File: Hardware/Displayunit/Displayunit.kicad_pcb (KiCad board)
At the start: 4 copper layers, 155 x 64.8 mm, 137 parts, among them IC1 TSC2007, IC2 MX25LM51245GXDI00, IC3 IS66WVH8M8BLL-100B1LI_0, J1 615008138221, J2 615008138221, J3 54104-4031, J4 Conn_ARM_JTAG_SWD_20, J5 52271-0679, J6 Conn_02x06_Odd_Even, J7 WAGO_Klemmleiste_2-pol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

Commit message: PCB Prototypen Produktions Stand
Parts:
- removed C60, C61: 2u2, Capacitor_SMD:C_1210_3225Metric
- C62, C63: footprint Capacitor_SMD:C_1210_3225Metric -> Capacitor_SMD:C_0603_1608Metric
- U5: value TPS54160DGQR -> (none)
- moved R22 45.9 mm to (99.5, 87.3)
- moved C65 42.5 mm to (100.5, 84.8), turned to 270 degrees
- moved D7 37.8 mm to (96.1, 80.8), turned to 180 degrees
- moved C63 37.2 mm to (89.5, 80.5), turned to 90 degrees
- moved C62 35.9 mm to (89.4, 68.0), turned to 90 degrees
- moved R2 34.4 mm to (105.6, 74.3), turned to 270 degrees
- moved C64 32.3 mm to (100.4, 71.9), turned to 270 degrees
- moved D6 30.2 mm to (96.2, 67.6), turned to 180 degrees
- moved R21 30.1 mm to (99.4, 74.5)
- moved C37 7.92 mm to (97.0, 98.0), turned to 270 degrees
- moved R16 7.59 mm to (105.4, 86.2)
- moved C44 7.39 mm to (109.6, 87.0), turned to 0 degrees
- moved C58 6.36 mm to (98.7, 84.7), turned to 270 degrees
- moved C42 6.26 mm to (108.4, 74.8)
- moved C57 5.94 mm to (98.7, 71.9), turned to 270 degrees
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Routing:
- net GND: track 860.3 -> 895.1 mm, vias 99 -> 107
- net Net-(C40-Pad1): track 0.00 -> 17.7 mm, vias 0 -> 2
- net Net-(C41-Pad1): track 1.65 -> 16.5 mm, vias 0 -> 2
- net +3.3VA: track 154.3 -> 143.7 mm, vias 10 -> 11
- net PWR_Reset: track 0.00 -> 10.6 mm, vias 0 -> 2
- net Net-(R16-Pad2): track 1.91 -> 12.4 mm
- net +3V3: track 408.3 -> 400.6 mm, vias 36 -> 40
- net Net-(BT1-Pad1): track 41.3 -> 34.1 mm
- net +BATT: track 48.8 -> 55.3 mm
- net Net-(C27-Pad1): track 18.4 -> 24.3 mm
- net Net-(C38-Pad1): track 0.00 -> 5.72 mm
- net RESET: track 96.7 -> 101.5 mm, vias 5 -> 7
- net Net-(C57-Pad2): track 0.00 -> 4.58 mm
- net Net-(R14-Pad2): track 1.91 -> 6.46 mm
- net Net-(C58-Pad2): track 0.00 -> 4.35 mm
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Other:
- board text added: "(c) RFguy 03/2020"
- board text removed: "(c) RFguy 02/2020"

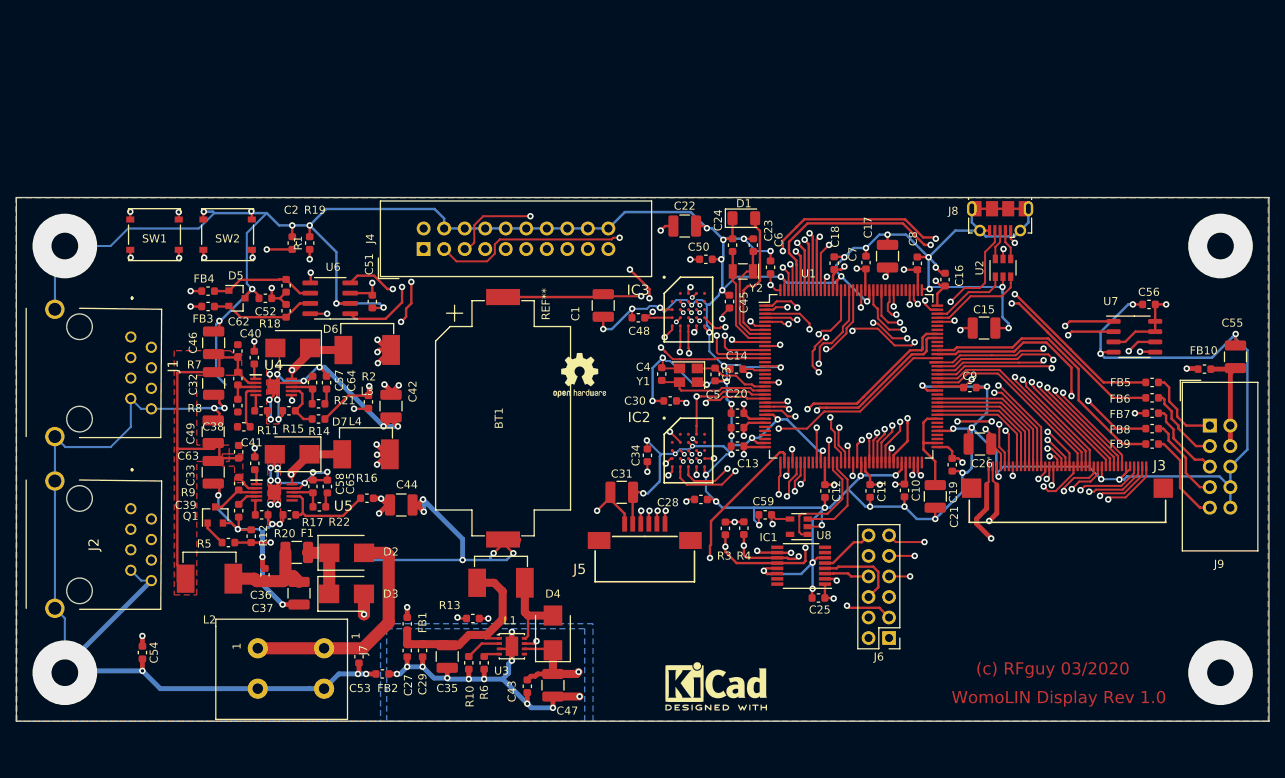
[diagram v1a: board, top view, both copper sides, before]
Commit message: Display Board: Fix JTAG REF, LED Treiber > TPS61165, Spulen zurück auf XAL4040 Footprint, Auf Version 2.0 gehoben
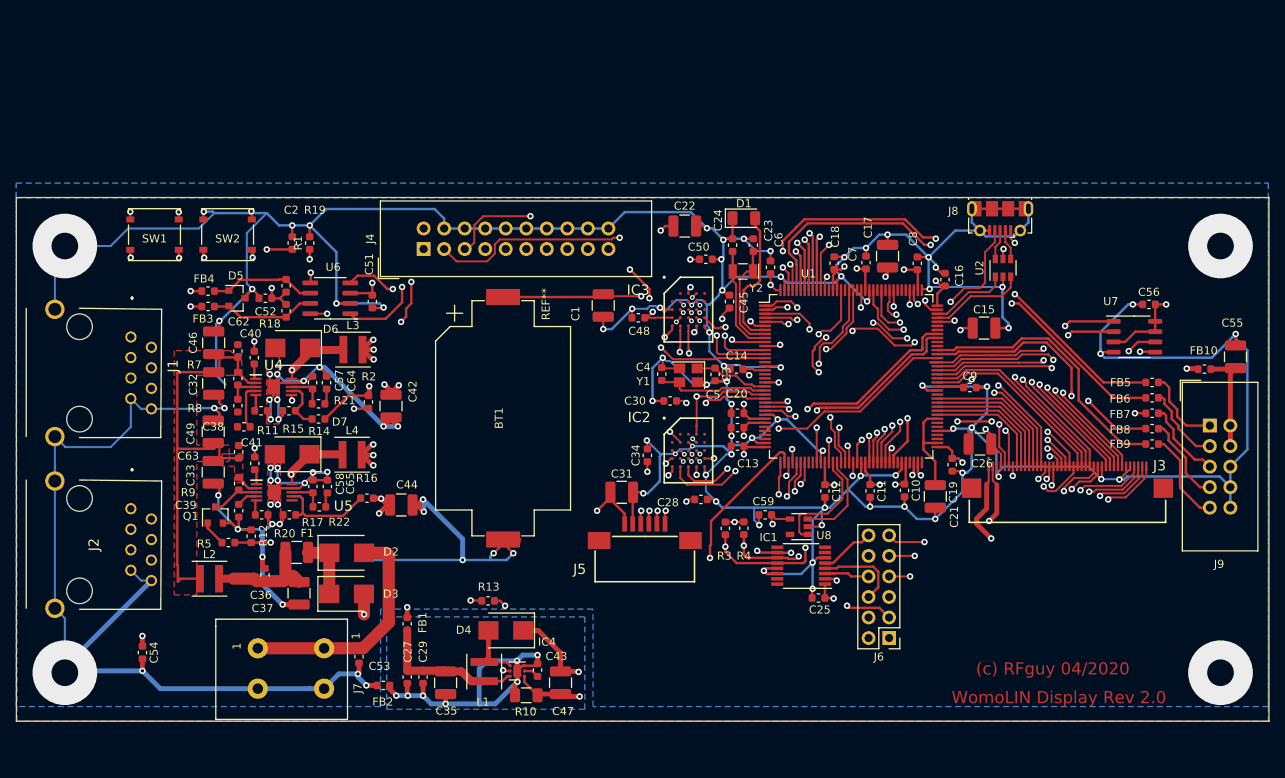
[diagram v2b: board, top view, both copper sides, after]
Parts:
- removed R6: 100K, Resistor_SMD:R_0603_1608Metric
- removed REF**: OSHW-Logo2_7.3x6mm_SilkScreen, Symbol:OSHW-Logo2_7.3x6mm_SilkScreen
- removed REF**: KiCad-Logo2_5mm_SilkScreen, Symbol:KiCad-Logo2_5mm_SilkScreen
- removed U3: STLD40D, Package_DFN_QFN:DFN-8-1EP_3x3mm_P0.65mm_EP1.55x2.4mm
- added IC4: TPS61165DRVR, Package_SON:WSON-6-1EP_2x2mm_P0.65mm_EP1x1.6mm, F.Cu at (124.0, 107.6)
- C1, C22, C31, C5, C55: value 1uF -> 1u
- C15: value 10uF -> 10u
- C16: value 10nF -> 10n
- C2, C28, C30, C34, C45, C48, C50: value 100nF -> 100n
- C43: value 10n -> 220n
- C46, C49: value 47u -> 10u
- C47: value 4u7 -> 1u
- D4: value B250 -> B260A-13-F
- L1: value 4uH7 -> 10uH; footprint Womo-Lin:MWSA0603 -> Inductor_SMD:L_Coilcraft_XxL4020
- L2: value L_Core_Ferrite -> 2uH2; footprint Womo-Lin:MWSA0603 -> Inductor_SMD:L_Coilcraft_XxL4020
- L3, L4: footprint Womo-Lin:MWSA0603 -> Inductor_SMD:L_Coilcraft_XxL4020
- R10: value 10R 1% -> 1R1; footprint Resistor_SMD:R_0603_1608Metric -> Resistor_SMD:R_1206_3216Metric
- R13: value 32k4 -> 10K
- U5: value (none) -> TPS54160DGQR
- moved L1 11.2 mm to (119.9, 107.7), turned to 90 degrees
- moved R10 8.17 mm to (125.1, 110.6), turned to 180 degrees
- moved D4 5.84 mm to (122.6, 102.6), turned to 180 degrees
- moved C29 3.28 mm to (112.3, 108.3)
- moved C27 3.28 mm to (110.4, 108.3)
- moved C35 3.25 mm to (115.1, 109.0)
- moved R13 2.88 mm to (120.4, 98.9)
- moved C43 2.37 mm to (126.5, 107.5), turned to 90 degrees
- moved L3 1.77 mm to (103.6, 67.8)
- moved L4 1.71 mm to (103.5, 80.8)
- moved FB2 1.43 mm to (107.4, 109.4)
- moved C47 0.99 mm to (129.3, 109.0)
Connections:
- C27 pad 2: LCD_LED-K -> Net-(C27-Pad2)
- C29 pad 2: LCD_LED-K -> Net-(C27-Pad2)
- C35 pad 2: LCD_LED-K -> Net-(C27-Pad2)
- C43 pad 1: LCD_LED-A -> Net-(C43-Pad1)
- C43 pad 2: LCD_LED-K -> Net-(C27-Pad2)
- FB2 pad 2: LCD_LED-K -> Net-(C27-Pad2)
- J4 pad 1: Net-(J4-Pad1) -> +3V3
- R10 pad 1: Net-(R10-Pad1) -> LCD_LED-K
- R10 pad 2: LCD_LED-K -> Net-(C27-Pad2)
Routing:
- net Net-(C27-Pad2): track 0.00 -> 43.1 mm, vias 0 -> 7
- net LCD_LED-K: track 121.8 -> 83.4 mm, vias 12 -> 2
- net Net-(C27-Pad1): track 24.3 -> 18.5 mm
- net Net-(R10-Pad1): track 4.44 -> 0.00 mm
- net LCD_BL_CTRL: track 54.0 -> 57.0 mm
- net LCD_LED-A: track 84.7 -> 81.7 mm
- net +BATT: track 55.3 -> 58.2 mm
- net Net-(D4-Pad2): track 10.4 -> 7.52 mm
- net Net-(R6-Pad1): track 2.00 -> 0.00 mm
- net Net-(C43-Pad1): track 0.00 -> 1.90 mm
- net Net-(C36-Pad1): track 12.1 -> 13.9 mm
- net +3.3VA: track 143.7 -> 142.4 mm
- net +3V3: track 400.6 -> 399.5 mm
- net GND: track 895.1 -> 896.1 mm
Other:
- board text added: "(c) RFguy 04/2020"
- board text added: "WomoLIN Display Rev 2.0"
- board text removed: "(c) RFguy 03/2020"
- board text removed: "WomoLIN Display Rev 1.0"

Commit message: Fix Lib gedrehte FPC Stecker, 10 Pin FPC hinzu gefügt (Buydisplay.com Alternative) Displayboard RS485 und CAN Option hinzu. Beginn Änderung Layout.
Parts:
- added C60: 100n, Capacitor_SMD:C_0603_1608Metric, F.Cu at (153.7, 36.2)
- added D8: NUP2105L, Package_TO_SOT_SMD:SOT-23, F.Cu at (140.0, 39.8)
- added FB11: 100R, Inductor_SMD:L_0603_1608Metric, F.Cu at (144.3, 38.8)
- added FB12: 100R, Inductor_SMD:L_0603_1608Metric, F.Cu at (162.2, 29.8)
- added J10: ER-CON10HT-1, Womo-Lin:ER-CON10HT-1, F.Cu at (144.8, 33.0)
- added R23: 0R, Resistor_SMD:R_0603_1608Metric, F.Cu at (144.3, 41.3)
- added R24: 0R, Resistor_SMD:R_0603_1608Metric, F.Cu at (153.7, 38.7)
- added R25: 0R, Resistor_SMD:R_0603_1608Metric, F.Cu at (148.3, 41.3)
- added R26: 120R, Resistor_SMD:R_0603_1608Metric, F.Cu at (157.7, 36.2)
- added R6: 0R, Resistor_SMD:R_0603_1608Metric, F.Cu at (148.3, 38.8)
- added U3: HD588E, Package_SO:SOIC-8_3.9x4.9mm_P1.27mm, F.Cu at (155.9, 31.7)
- IC4: footprint Package_SON:WSON-6-1EP_2x2mm_P0.65mm_EP1x1.6mm -> Package_SON:WSON-6-1EP_2x2mm_P0.65mm_EP1x1.6mm_ThermalVias
- L1, L2, L3, L4: footprint Inductor_SMD:L_Coilcraft_XxL4020 -> Womo-Lin:MWSA0603
- U7: footprint Package_SO:SO-8_3.9x4.9mm_P1.27mm -> Package_SO:SO-8_5.3x6.2mm_P1.27mm
- moved C26 26.2 mm to (201.8, 95.7)
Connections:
- C10 pad 1: +3V3 -> Net-(C10-Pad1)
- C17 pad 1: +3V3 -> Net-(C17-Pad1)
- C18 pad 2: +3V3 -> Net-(C17-Pad1)
- C19 pad 2: +3V3 -> Net-(C17-Pad1)
- C20 pad 2: +3V3 -> Net-(C17-Pad1)
- IC1 pad 13: GND -> Net-(IC1-Pad13)
- IC1 pad 14: GND -> Net-(IC1-Pad13)
- J1 pad 3: Net-(J1-Pad3) -> Net-(FB11-Pad1)
- J1 pad 6: Net-(J1-Pad6) -> Net-(FB11-Pad1)
- J2 pad 6: Net-(J2-Pad6) -> Net-(FB11-Pad1)
- U1 pad 108: +3V3 -> Net-(U1-Pad108)
- U1 pad 131: +3V3 -> Net-(C17-Pad1)
- U1 pad 139: EXT_1 -> CAN1_RX
- U1 pad 140: EXT_2 -> CAN1_TX
- U1 pad 30: +3V3 -> Net-(C17-Pad1)
- U1 pad 31: Net-(U1-Pad31) -> USART2_CTS_NSS
- U1 pad 32: Net-(U1-Pad32) -> USART2_RTS_DE
- U1 pad 33: Net-(U1-Pad33) -> USART2_TX
- U1 pad 34: Net-(U1-Pad34) -> USART2_RX
- U1 pad 65: EXT_3 -> EXT_1
- U1 pad 66: Net-(U1-Pad66) -> EXT_2
- U1 pad 68: +3V3 -> Net-(U1-Pad68)
- U1 pad 69: Net-(U1-Pad69) -> EXT_3
- U1 pad 73: +3V3 -> Net-(C17-Pad1)
- U6 pad 1: USART1_TX -> Net-(R23-Pad1)
- U6 pad 4: USART1_RX -> Net-(R24-Pad1)
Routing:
- net EXT_2: track 60.4 -> 10.8 mm, vias 2 -> 0
- net CAN1_RX: track 0.00 -> 42.2 mm, vias 0 -> 4
- net CAN1_TX: track 0.00 -> 39.9 mm, vias 0 -> 2
- net EXT_3: track 38.5 -> 1.83 mm, vias 4 -> 1
- net LCD_R2: track 19.5 -> 38.5 mm
- net LCD_LED-A: track 81.7 -> 99.7 mm
- net LCD_LED-K: track 83.4 -> 101.2 mm
- net LCD_40: track 36.8 -> 19.8 mm
- net LCD_39: track 37.5 -> 21.1 mm
- net LCD_38: track 39.8 -> 25.6 mm
- net LCD_37: track 40.3 -> 26.2 mm
- net LCD_R0: track 50.5 -> 63.6 mm
- net LCD_R3: track 14.9 -> 26.8 mm, vias 0 -> 2
- net LCD_R1: track 51.1 -> 62.8 mm
- net LCD_R4: track 15.6 -> 27.1 mm, vias 0 -> 2
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
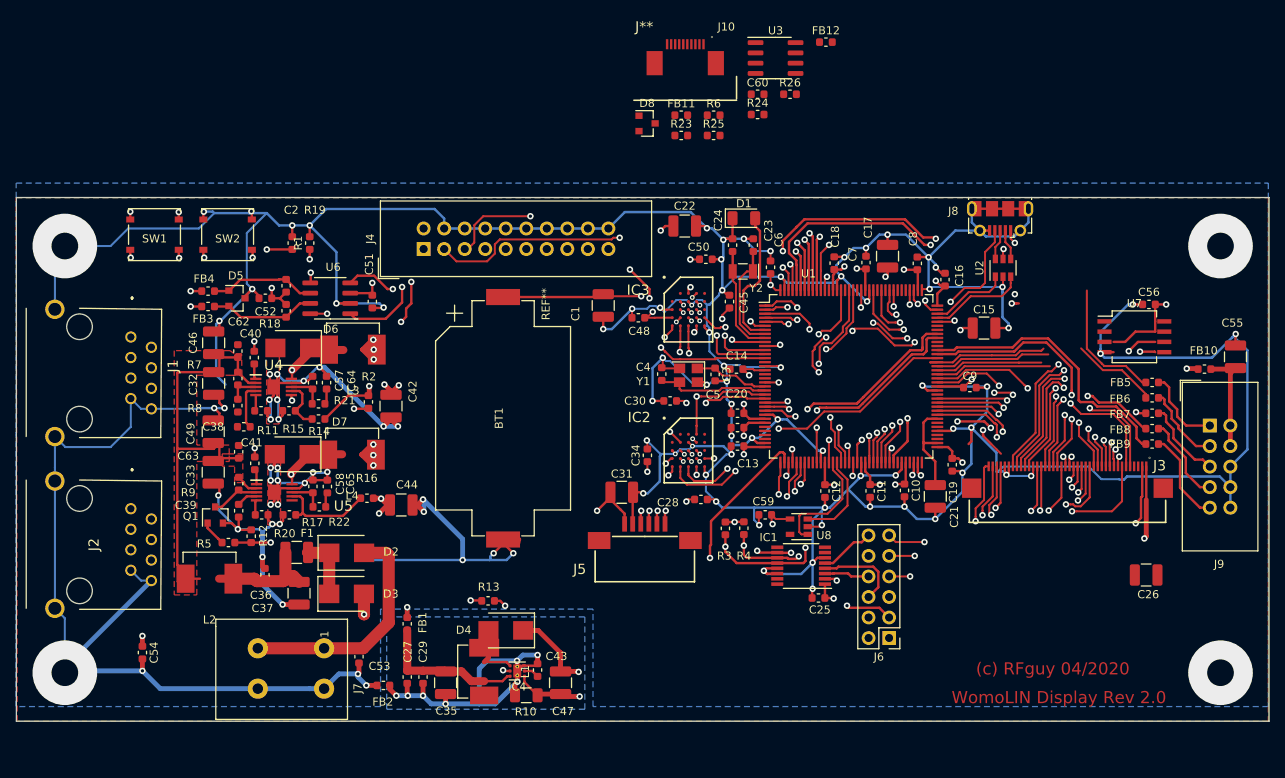
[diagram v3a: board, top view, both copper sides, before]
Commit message: Fix Womolin Lib, ein paar Bauteile fehlte Lötstopmaske. Displayboard stand zweite Prototyp Bestellung.
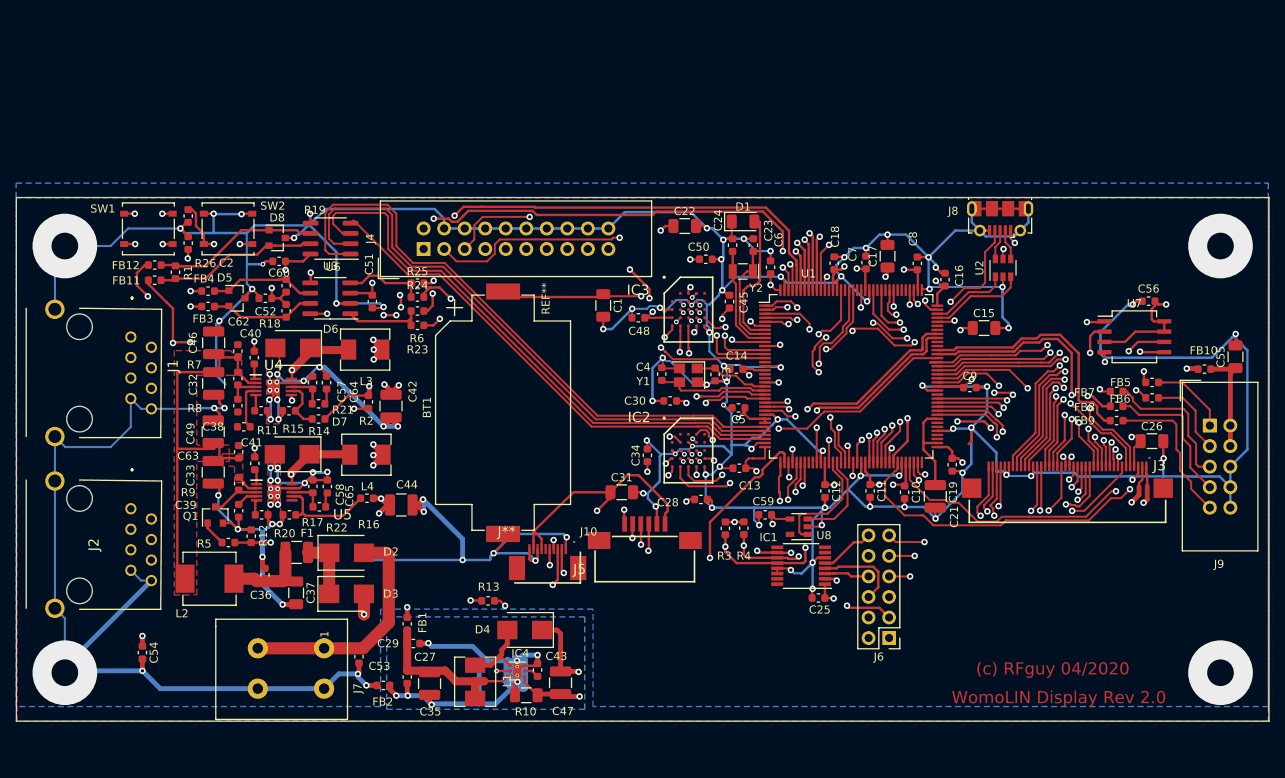
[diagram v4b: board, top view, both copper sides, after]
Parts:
- removed C20: 100n, Capacitor_SMD:C_0603_1608Metric
- C1, C15, C17, C22, C26, C31, C37, C55: footprint Capacitor_SMD:C_1210_3225Metric -> Capacitor_SMD:C_1206_3216Metric
- FB5, FB6, FB7, FB8, FB9: value BLM18PG121SN1D -> 100r
- L1, L3, L4: footprint Womo-Lin:MWSA0603 -> Womo-Lin:MWSA0503
- R1, R13, R15, R2, R3, R4: value 10K -> 10k
- R14: value 31K6 -> 31k6
- moved FB12 87.5 mm to (79.1, 57.4)
- moved R26 79.2 mm to (81.7, 58.2), turned to 90 degrees
- moved FB11 68.3 mm to (79.1, 59.2)
- moved J10 64.8 mm to (127.7, 95.4)
- moved C60 62.7 mm to (94.5, 56.9), turned to 180 degrees
- moved U3 59.4 mm to (100.9, 54.1), turned to 180 degrees
- moved D8 47.9 mm to (94.3, 54.0)
- moved R24 47.8 mm to (111.6, 61.3)
- moved R6 43.9 mm to (111.6, 63.0)
- moved R25 40.9 mm to (111.6, 59.6)
- moved R23 40.2 mm to (111.6, 64.8)
- moved C26 16.6 mm to (202.5, 79.1), turned to 0 degrees
- moved R1 15.0 mm to (83.3, 54.6)
- moved C2 13.3 mm to (83.3, 51.3), turned to 270 degrees
- moved FB9 5.26 mm to (198.1, 76.6)
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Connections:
- C10 pad 1: Net-(C10-Pad1) -> +3V3
- C17 pad 1: Net-(C17-Pad1) -> +3V3
- C18 pad 2: Net-(C17-Pad1) -> +3V3
- C19 pad 2: Net-(C17-Pad1) -> +3V3
- IC1 pad 13: Net-(IC1-Pad13) -> GND
- IC1 pad 14: Net-(IC1-Pad13) -> GND
- J1 pad 3: Net-(FB11-Pad1) -> Net-(FB12-Pad1)
- U1 pad 108: Net-(U1-Pad108) -> +3V3
- U1 pad 131: Net-(C17-Pad1) -> +3V3
- U1 pad 30: Net-(C17-Pad1) -> +3V3
- U1 pad 68: Net-(U1-Pad68) -> +3V3
- U1 pad 73: Net-(C17-Pad1) -> +3V3
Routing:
- net USART2_CTS_NSS: track 0.00 -> 77.3 mm
- net USART2_RTS_DE: track 0.00 -> 74.0 mm
- net USART2_TX: track 0.00 -> 71.0 mm
- net USART2_RX: track 0.00 -> 62.6 mm
- net Net-(FB11-Pad1): track 0.00 -> 47.1 mm, vias 0 -> 2
- net EXT_3: track 1.83 -> 48.0 mm, vias 1 -> 2
- net EXT_2: track 10.8 -> 53.2 mm, vias 0 -> 2
- net +3.3VA: track 140.6 -> 182.9 mm
- net Net-(FB12-Pad1): track 0.00 -> 36.2 mm, vias 0 -> 1
- net GND: track 896.2 -> 922.7 mm, vias 106 -> 119
- net CAN1_TX: track 39.9 -> 64.4 mm
- net CAN1_RX: track 42.2 -> 63.4 mm
- net Net-(D8-Pad1): track 0.00 -> 20.6 mm
- net Net-(D8-Pad2): track 0.00 -> 20.4 mm
- net Net-(C27-Pad2): track 43.1 -> 63.1 mm
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- added copper zone on B.Cu, net Net-(C27-Pad2)
- removed copper zone on B.Cu, net LCD_LED-K

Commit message: Displayunit: Kleiner Fix Mainboard: Netzteil Sektion komplett auf TI umgestellt, Footprints angepasst. Victron kompatible TTY Ports platziert und gerouted, auf Version 2.0 gehoben.
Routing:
- net Net-(C41-Pad1): track 16.5 -> 17.4 mm
